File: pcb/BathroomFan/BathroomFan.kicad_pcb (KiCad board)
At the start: 2 copper layers, 76 x 106 mm, 16 parts, among them J1 Screw_Terminal_01x02, J2 Screw_Terminal_01x02, SW1 SW_SPST, U1 ESP32-DEVKIT-V1, U2 DHT11, U3 AC/DC Module 5V 700mA

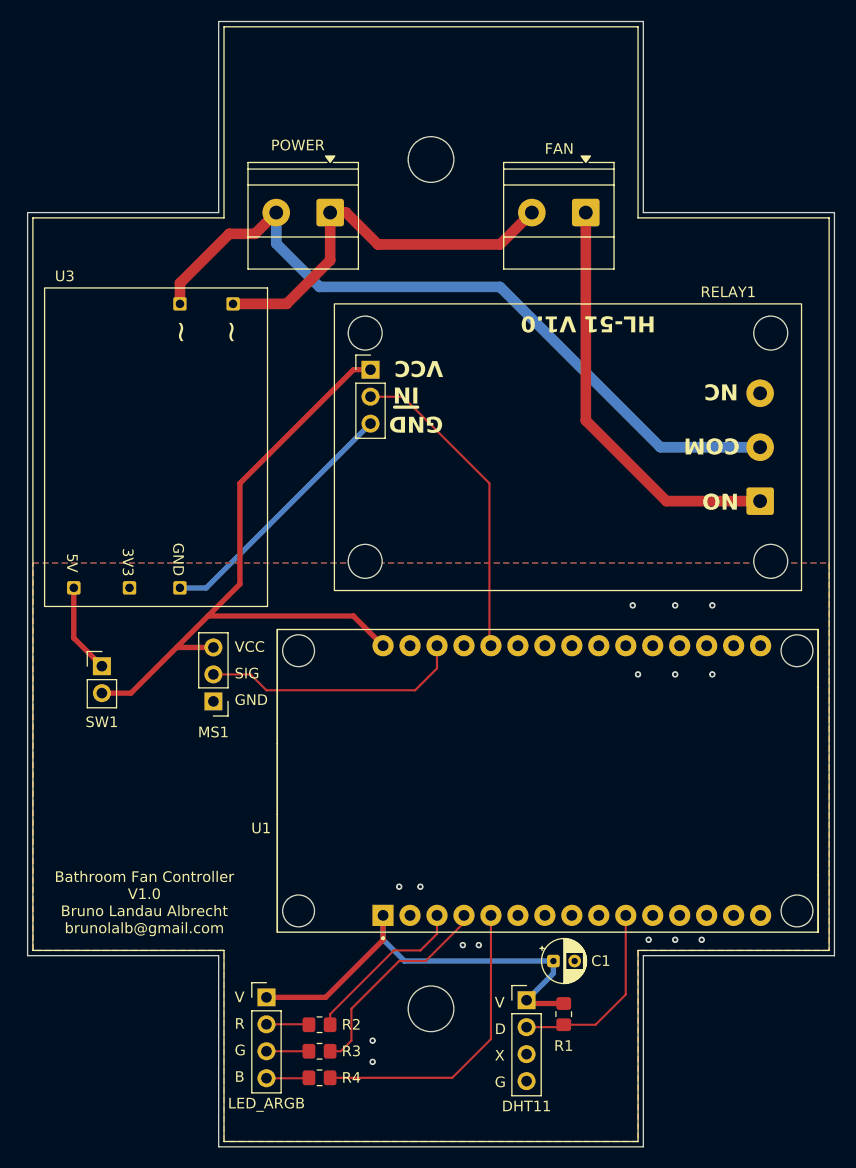
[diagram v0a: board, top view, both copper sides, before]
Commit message: SCH and PCB: added logo, adjusted silk identifier
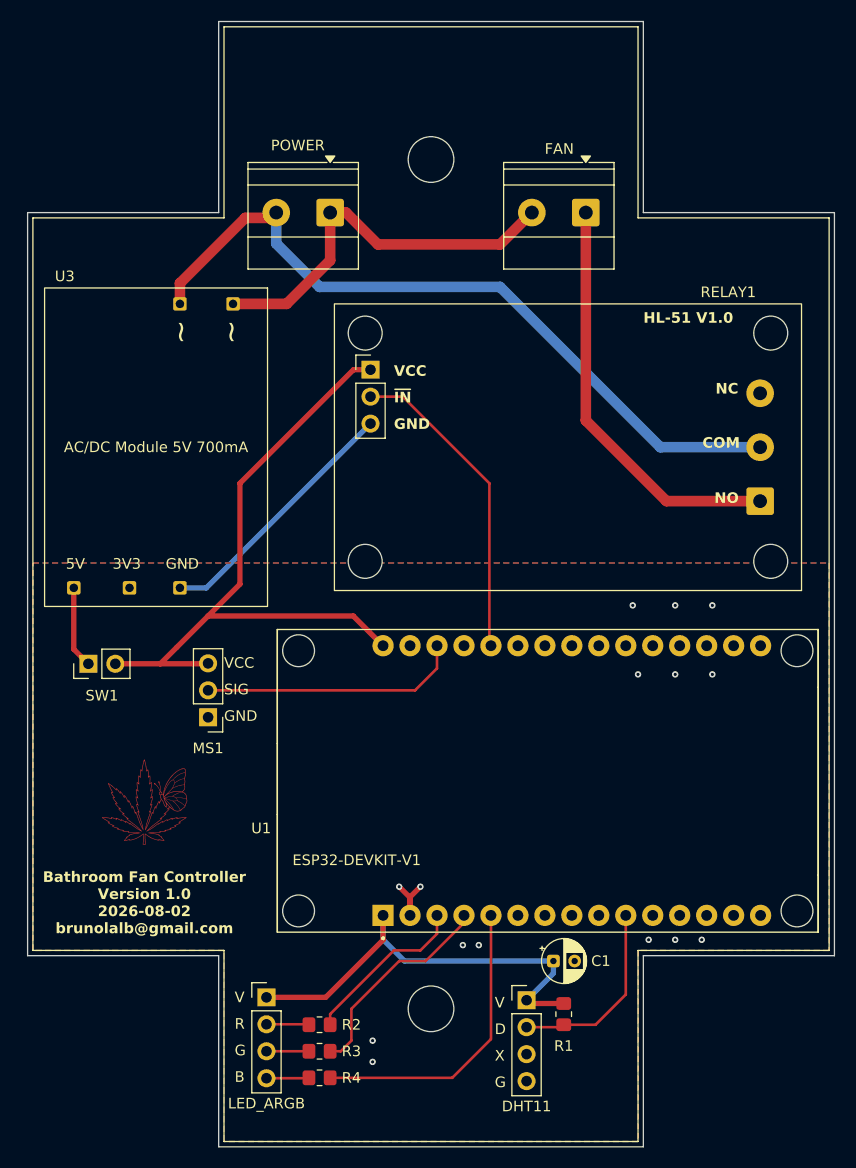
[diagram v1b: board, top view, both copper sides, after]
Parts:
- added G1: LOGO, bathroom_fan:LOGO, F.Cu at (143.0, 117.6)
- moved MS1 1.58 mm to (149.0, 109.5)
- moved SW1 1.29 mm to (137.7, 104.5), turned to 90 degrees
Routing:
- net GND: track 24.4 -> 30.6 mm
- net +5V: track 64.6 -> 63.2 mm
- net +5V_pre: track 8.47 -> 7.72 mm
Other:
- board text added: "${TITLE} Version ${REVISION} ${ISSUE_DATE} ${COMPANY}"
- board text removed: "Bathroom Fan Controller V${REVISION} ${COMMENT1} ${COMPANY}"
